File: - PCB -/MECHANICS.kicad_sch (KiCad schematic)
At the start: 4 parts, among them SW1 SW_SPDT

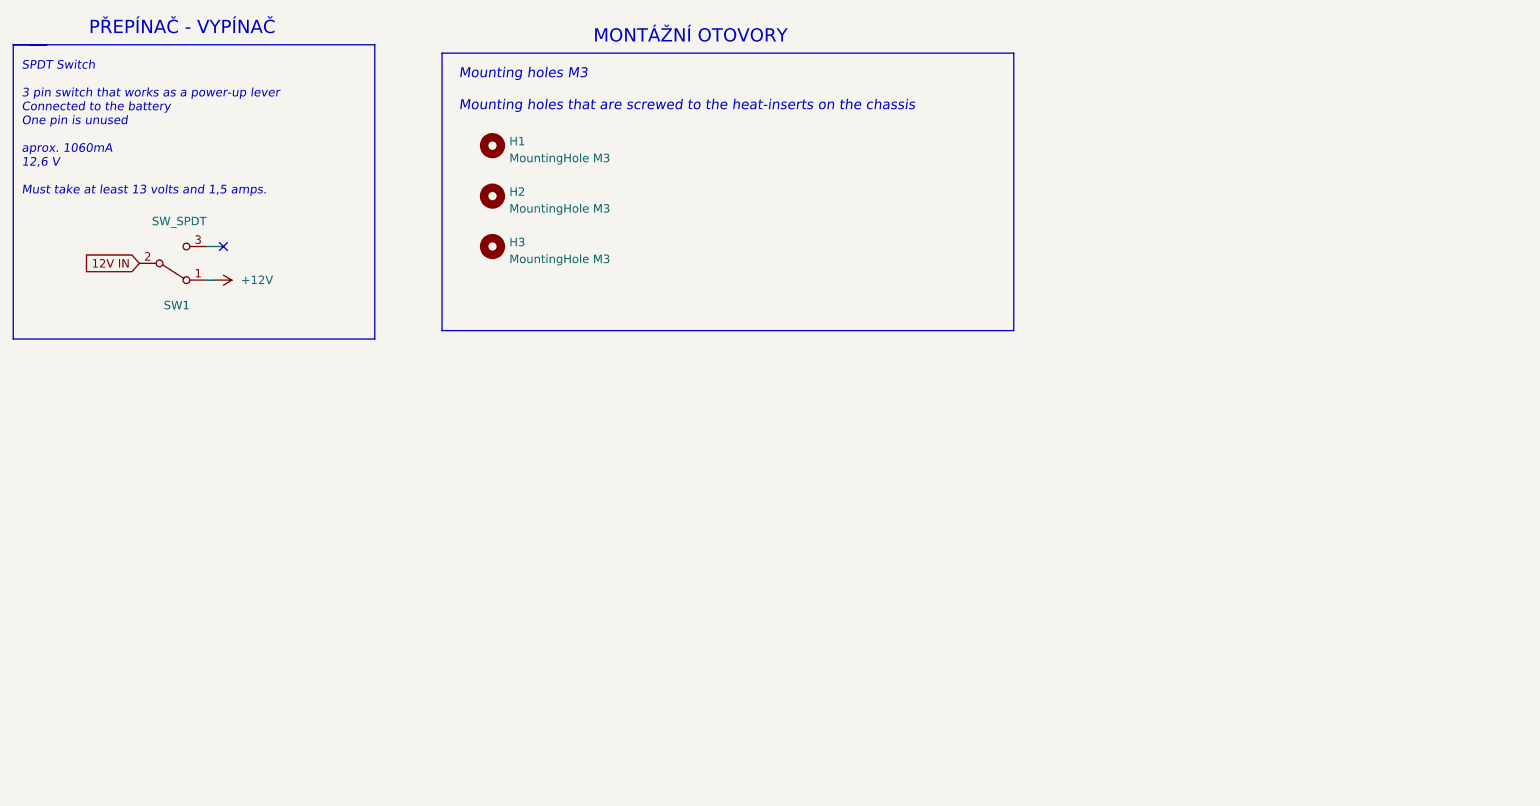
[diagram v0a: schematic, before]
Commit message: PCB - SCH UPDATE (fully labelled and described)
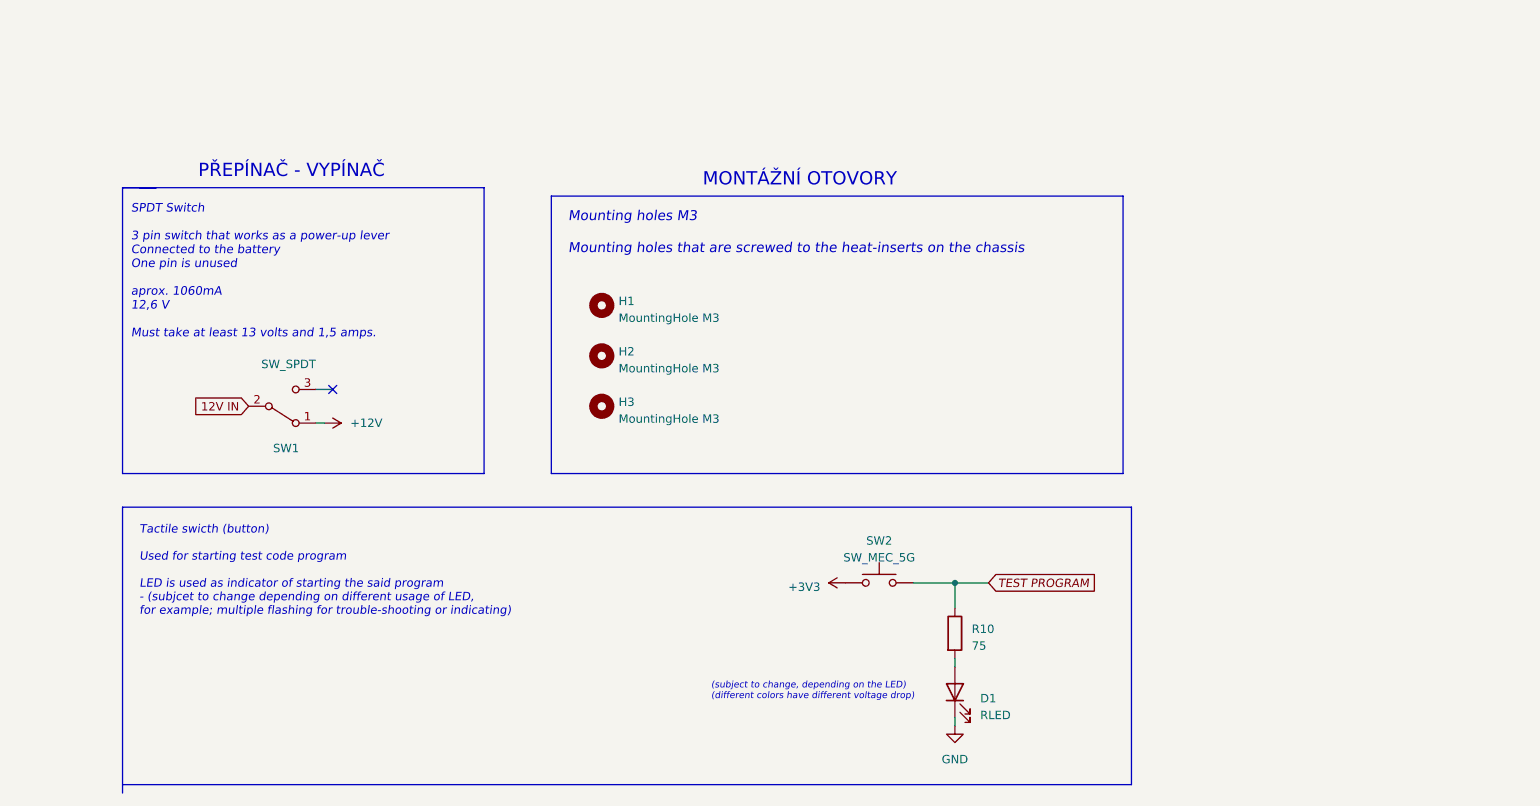
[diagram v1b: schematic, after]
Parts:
- added D1: RLED, symbol Device:LED
- added R10: 75, symbol Device:R
- added SW2: SW_MEC_5G, symbol Switch:SW_MEC_5G
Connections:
- new net: D1.2 (A), R10.2
- new net +3V3: SW2.1 (A), SW2.2 (A)
- new net GND: D1.1 (K)
- new net TEST PROGRAM: R10.1, SW2.3 (B), SW2.4 (B)
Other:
- note added: "(subject to change, depending on the LED) (different colors have different voltage drop)"
- note added: "Tactile swicth (button) Used for starting test code program LED is used as indicator of starting the said program - (subjcet to change depending on different usage of LED, for example; multiple flashing for trouble-shooting or indicating)"
- moved on the sheet: H1, H2, H3, SW1

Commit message: PCB - sch and footprint update, QRE1113 3D model.
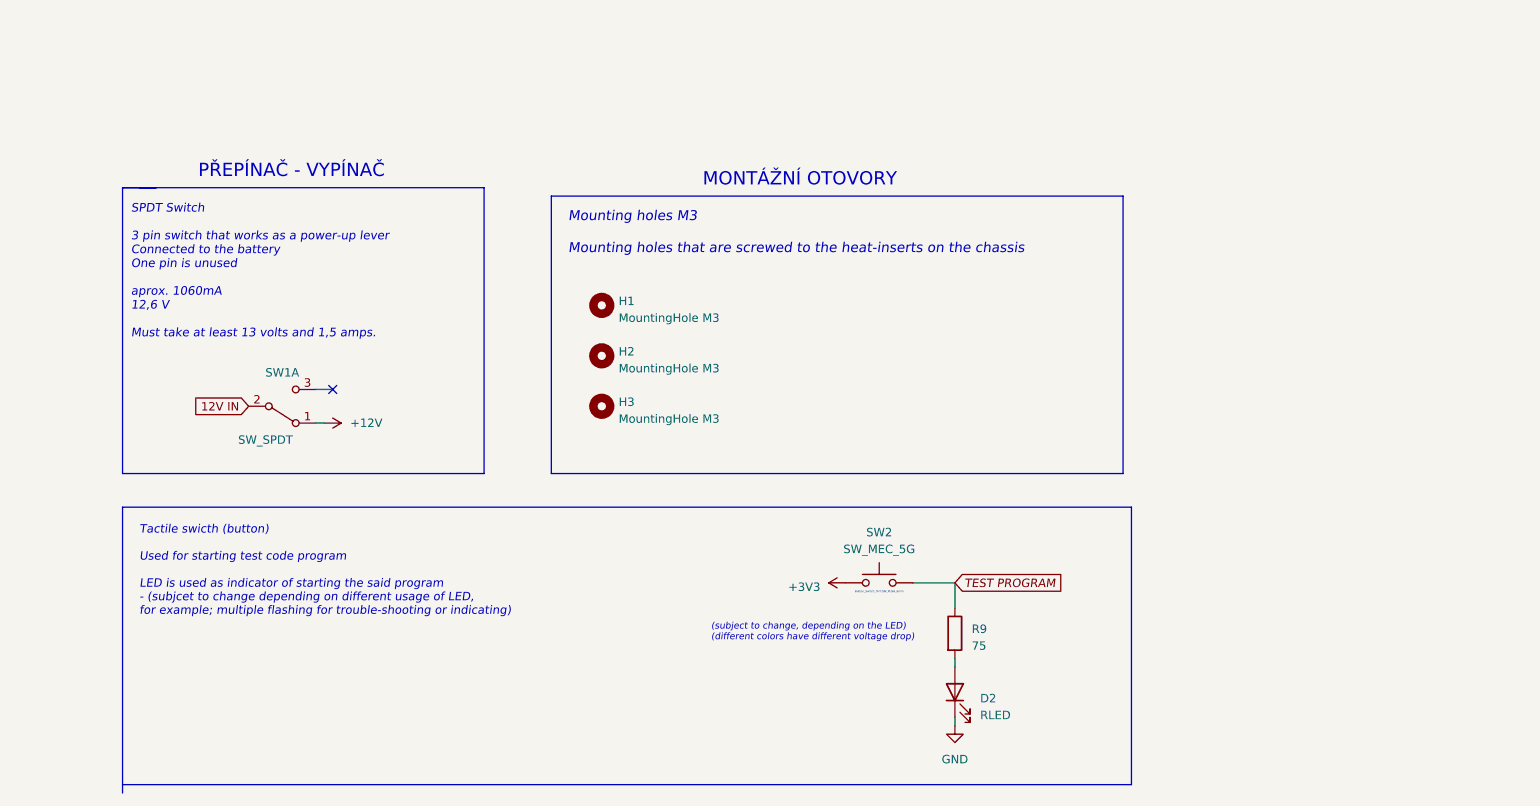
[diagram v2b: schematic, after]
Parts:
- removed SW1: SW_SPDT, SWITCH:SW_100SP1T1B4M2QE, symbol Switch:SW_SPDT
- added SW1: SW_SPDT, SWITCH SPDT:SW_100SP1T1B4M2QE, symbol Switch:SW_DPDT_x2
- D2: renamed from D1; footprint (none) -> LED_THT:LED_D5.0mm
- R9: renamed from R10; footprint (none) -> Resistor_THT:R_Axial_DIN0207_L6.3mm_D2.5mm_P10.16mm_Horizontal
- SW2: footprint (none) -> Button_Switch_THT:SW_PUSH_6mm
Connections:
- net +12V: now also SW1.1 (A)
- net 12V IN: now also SW1.2 (B)
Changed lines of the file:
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@@
 (kicad_sch (version 20230121) (generator eeschema)
   (paper "A4")
-  (junction (at 191.77 127) (diameter 0) (color 0 0 0 0)
-  )
   (no_connect (at 97.79 97.79))
   (polyline (pts (xy 66.04 115.57) (xy 218.44 115.57))
     (stroke (width 0) (type default))
   )
-  (wire (pts (xy 191.77 130.81) (xy 191.77 127))
-    (stroke (width 0) (type default))
-  )
   (wire (pts (xy 191.77 147.32) (xy 191.77 148.59))
     (stroke (width 0) (type default))
@@
     (stroke (width 0) (type default))
   )
+  (wire (pts (xy 191.77 127) (xy 191.77 130.81))
+    (stroke (width 0) (type default))
+  )
   (polyline (pts (xy 130.81 68.58) (xy 217.17 68.58))
     (stroke (width 0) (type default))
   )
   (wire (pts (xy 191.77 127) (xy 185.42 127))
-    (stroke (width 0) (type default))
-  )
-  (wire (pts (xy 196.85 127) (xy 191.77 127))
     (stroke (width 0) (type default))
   )
@@
   )
   (text "(subject to change, depending on the LED)\n(different colors have different voltage drop)"
-    (at 154.94 144.78 0)
+    (at 154.94 135.89 0)
     (effects (font (size 1 1) italic) (justify left bottom))
   )
-  (global_label "TEST PROGRAM" (shape input) (at 196.85 127 0) (fields_autoplaced)
+  (global_label "TEST PROGRAM" (shape input) (at 191.77 127 0) (fields_autoplaced)
     (effects (font (size 1.27 1.27) italic) (justify left))
-    (property "Intersheetrefs" "${INTERSHEET_REFS}" (at 213.8845 127 0)
+    (property "Intersheetrefs" "${INTERSHEET_REFS}" (at 208.8045 127 0)
       (effects (font (size 1.27 1.27)) (justify left) hide)
     )
@@
   )
   (symbol (lib_id "Switch:SW_MEC_5G") (at 180.34 127 0) (unit 1)
-    (in_bom yes) (on_board yes) (dnp no) (fields_autoplaced)
-    (property "Reference" "SW2" (at 180.34 120.65 0)
-      (effects (font (size 1.27 1.27)))
-    )
-    (property "Value" "SW_MEC_5G" (at 180.34 123.19 0)
-      (effects (font (size 1.27 1.27)))
-    )
-    (property "Footprint" "" (at 180.34 121.92 0)
-      (effects (font (size 1.27 1.27)) hide)
+    (in_bom yes) (on_board yes) (dnp no)
+    (property "Reference" "SW2" (at 180.34 119.38 0)
+      (effects (font (size 1.27 1.27)))
+    )
+    (property "Value" "SW_MEC_5G" (at 180.34 121.92 0)
+      (effects (font (size 1.27 1.27)))
+    )
+    (property "Footprint" "Button_Switch_THT:SW_PUSH_6mm" (at 180.34 128.27 0)
+      (effects (font (size 0.3 0.3)))
     )
     (property "Datasheet" "http://www.apem.com/int/index.php?controller=attachment&id_attachment=488" (at 180.34 121.92 0)
@@
   (symbol (lib_id "Device:R") (at 191.77 134.62 0) (unit 1)
     (in_bom yes) (on_board yes) (dnp no) (fields_autoplaced)
-    (property "Reference" "R10" (at 194.31 133.985 0)
+    (property "Reference" "R9" (at 194.31 133.985 0)
       (effects (font (size 1.27 1.27)) (justify left))
     )
@@
       (effects (font (size 1.27 1.27)) (justify left))
     )
-    (property "Footprint" "" (at 189.992 134.62 90)
+    (property "Footprint" "Resistor_THT:R_Axial_DIN0207_L6.3mm_D2.5mm_P10.16mm_Horizontal" (at 189.992 134.62 90)
       (effects (font (size 1.27 1.27)) hide)
     )
@@
       (project "sumec"
         (path "/fc70a1a8-ed7c-4a0f-9b1a-f23293528385/05a35bad-c108-46ad-8f95-76319a60a14f"
-          (reference "R10") (unit 1)
-        )
-      )
-    )
-  )
-  (symbol (lib_id "Switch:SW_SPDT") (at 90.17 100.33 0) (mirror x) (unit 1)
-    (in_bom yes) (on_board yes) (dnp no)
-    (property "Reference" "SW1" (at 92.71 106.68 0)
-      (effects (font (size 1.27 1.27)) (justify right))
-    )
-    (property "Value" "SW_SPDT" (at 95.25 93.98 0)
-      (effects (font (size 1.27 1.27)) (justify right))
-    )
-    (property "Footprint" "SWITCH:SW_100SP1T1B4M2QE" (at 90.17 100.33 0)
-      (effects (font (size 1.27 1.27)) hide)
-    )
-    (property "Datasheet" "~" (at 90.17 100.33 0)
-      (effects (font (size 1.27 1.27)) hide)
-    )
-    (pin "1")
-    (pin "2")
-    (pin "3")
-    (instances
-      (project "sumec"
-        (path "/fc70a1a8-ed7c-4a0f-9b1a-f23293528385"
-          (reference "SW1") (unit 1)
-        )
-        (path "/fc70a1a8-ed7c-4a0f-9b1a-f23293528385/05a35bad-c108-46ad-8f95-76319a60a14f"
-          (reference "SW1") (unit 1)
+          (reference "R9") (unit 1)
         )
       )
@@
     )
   )
+  (symbol (lib_id "Switch:SW_DPDT_x2") (at 90.17 100.33 0) (mirror x) (unit 1)
+    (in_bom yes) (on_board yes) (dnp no)
+    (property "Reference" "SW1" (at 90.17 95.25 0)
+      (effects (font (size 1.27 1.27)))
+    )
+    (property "Value" "SW_SPDT" (at 87.63 105.41 0)
+      (effects (font (size 1.27 1.27)))
+    )
+    (property "Footprint" "SWITCH SPDT:SW_100SP1T1B4M2QE" (at 90.17 100.33 0)
+      (effects (font (size 1.27 1.27)) hide)
+    )
+    (property "Datasheet" "~" (at 90.17 100.33 0)
+      (effects (font (size 1.27 1.27)) hide)
+    )
+    (pin "1")
+    (pin "2")
+    (pin "3")
+    (pin "4")
+    (pin "5")
+    (pin "6")
+    (instances
+      (project "sumec"
+        (path "/fc70a1a8-ed7c-4a0f-9b1a-f23293528385/05a35bad-c108-46ad-8f95-76319a60a14f"
+          (reference "SW1") (unit 1)
+        )
+      )
+    )
+  )
   (symbol (lib_id "Device:LED") (at 191.77 143.51 90) (unit 1)
     (in_bom yes) (on_board yes) (dnp no) (fields_autoplaced)
-    (property "Reference" "D1" (at 195.58 144.4625 90)
+    (property "Reference" "D2" (at 195.58 144.4625 90)
       (effects (font (size 1.27 1.27)) (justify right))
     )
@@
       (effects (font (size 1.27 1.27)) (justify right))
     )
-    (property "Footprint" "" (at 191.77 143.51 0)
+    (property "Footprint" "LED_THT:LED_D5.0mm" (at 191.77 143.51 0)
       (effects (font (size 1.27 1.27)) hide)
     )
@@
       (project "sumec"
         (path "/fc70a1a8-ed7c-4a0f-9b1a-f23293528385/05a35bad-c108-46ad-8f95-76319a60a14f"
-          (reference "D1") (unit 1)
-        )
-      )
+          (reference "D2") (unit 1)
+        )
+      )

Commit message: PCB - board update + footprint/3d models export
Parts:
- removed SW2: SW_MEC_5G, Button_Switch_THT:SW_PUSH_6mm, symbol Switch:SW_MEC_5G
- added SW3: SW_Push, Button_Switch_THT:SW_PUSH_6mm, symbol Switch:SW_Push
- SW1: footprint SWITCH SPDT:SW_100SP1T1B4M2QE -> Connector_JST:JST_EH_B3B-EH-A_1x03_P2.50mm_Vertical
- renumbered D2 to D1, H2 to H?, H3 to H?, H1 to H?, R9 to R1
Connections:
- net +3V3: now also SW3.1
- net TEST PROGRAM: now also SW3.2

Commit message: Board update
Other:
- note added: "^ (subject to change, depending on the LED) (different colors have different voltage drop)"
- note removed: "(subject to change, depending on the LED) (different colors have different voltage drop)"
- moved on the sheet: D1, R1, SW3
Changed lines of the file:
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@@
 (kicad_sch (version 20230121) (generator eeschema)
   (paper "A4")
+  (junction (at 173.99 139.7) (diameter 0) (color 0 0 0 0)
+  )
   (no_connect (at 97.79 97.79))
   (polyline (pts (xy 66.04 115.57) (xy 218.44 115.57))
     (stroke (width 0) (type default))
   )
-  (wire (pts (xy 191.77 147.32) (xy 191.77 148.59))
+  (wire (pts (xy 193.04 139.7) (xy 194.31 139.7))
     (stroke (width 0) (type default))
   )
@@
     (stroke (width 0) (type default))
   )
-  (wire (pts (xy 191.77 139.7) (xy 191.77 138.43))
-    (stroke (width 0) (type default))
-  )
-  (wire (pts (xy 191.77 127) (xy 191.77 130.81))
+  (wire (pts (xy 185.42 139.7) (xy 184.15 139.7))
     (stroke (width 0) (type default))
   )
@@
     (stroke (width 0) (type default))
   )
-  (wire (pts (xy 173.99 127) (xy 175.26 127))
+  (wire (pts (xy 161.29 139.7) (xy 162.56 139.7))
     (stroke (width 0) (type default))
   )
@@
     (stroke (width 0) (type default))
   )
-  (wire (pts (xy 191.77 127) (xy 185.42 127))
+  (wire (pts (xy 173.99 139.7) (xy 176.53 139.7))
+    (stroke (width 0) (type default))
+  )
+  (wire (pts (xy 172.72 139.7) (xy 173.99 139.7))
+    (stroke (width 0) (type default))
+  )
+  (wire (pts (xy 173.99 135.89) (xy 173.99 139.7))
     (stroke (width 0) (type default))
   )
@@
     (effects (font (size 1.27 1.27) italic) (justify left bottom))
   )
-  (text "(subject to change, depending on the LED)\n(different colors have different voltage drop)"
-    (at 154.94 135.89 0)
+  (text "                 ^\n(subject to change, depending on the LED)\n(different colors have different voltage drop)"
+    (at 167.64 146.05 0)
     (effects (font (size 1 1) italic) (justify left bottom))
   )
-  (global_label "TEST PROGRAM" (shape input) (at 191.77 127 0) (fields_autoplaced)
+  (global_label "TEST PROGRAM" (shape input) (at 173.99 135.89 90) (fields_autoplaced)
     (effects (font (size 1.27 1.27) italic) (justify left))
-    (property "Intersheetrefs" "${INTERSHEET_REFS}" (at 208.8045 127 0)
+    (property "Intersheetrefs" "${INTERSHEET_REFS}" (at 173.99 118.8555 90)
       (effects (font (size 1.27 1.27)) (justify left) hide)
     )
@@
     )
   )
-  (symbol (lib_id "power:GND") (at 191.77 148.59 0) (unit 1)
-    (in_bom yes) (on_board yes) (dnp no) (fields_autoplaced)
-    (property "Reference" "#PWR03" (at 191.77 154.94 0)
-      (effects (font (size 1.27 1.27)) hide)
-    )
-    (property "Value" "GND" (at 191.77 153.67 0)
-      (effects (font (size 1.27 1.27)))
-    )
-    (property "Footprint" "" (at 191.77 148.59 0)
-      (effects (font (size 1.27 1.27)) hide)
-    )
-    (property "Datasheet" "" (at 191.77 148.59 0)
+  (symbol (lib_id "power:GND") (at 194.31 139.7 90) (unit 1)
+    (in_bom yes) (on_board yes) (dnp no) (fields_autoplaced)
+    (property "Reference" "#PWR03" (at 200.66 139.7 0)
+      (effects (font (size 1.27 1.27)) hide)
+    )
+    (property "Value" "GND" (at 199.39 139.7 0)
+      (effects (font (size 1.27 1.27)))
+    )
+    (property "Footprint" "" (at 194.31 139.7 0)
+      (effects (font (size 1.27 1.27)) hide)
+    )
+    (property "Datasheet" "" (at 194.31 139.7 0)
       (effects (font (size 1.27 1.27)) hide)
     )
@@
     )
   )
-  (symbol (lib_id "Switch:SW_Push") (at 180.34 127 0) (unit 1)
-    (in_bom yes) (on_board yes) (dnp no) (fields_autoplaced)
-    (property "Reference" "SW3" (at 180.34 120.65 0)
-      (effects (font (size 1.27 1.27)))
-    )
-    (property "Value" "SW_Push" (at 180.34 123.19 0)
-      (effects (font (size 1.27 1.27)))
-    )
-    (property "Footprint" "Button_Switch_THT:SW_PUSH_6mm" (at 180.34 121.92 0)
-      (effects (font (size 1.27 1.27)) hide)
-    )
-    (property "Datasheet" "~" (at 180.34 121.92 0)
+  (symbol (lib_id "Switch:SW_Push") (at 167.64 139.7 0) (unit 1)
+    (in_bom yes) (on_board yes) (dnp no) (fields_autoplaced)
+    (property "Reference" "SW3" (at 167.64 133.35 0)
+      (effects (font (size 1.27 1.27)))
+    )
+    (property "Value" "SW_Push" (at 167.64 135.89 0)
+      (effects (font (size 1.27 1.27)))
+    )
+    (property "Footprint" "Button_Switch_THT:SW_PUSH_6mm" (at 167.64 134.62 0)
+      (effects (font (size 1.27 1.27)) hide)
+    )
+    (property "Datasheet" "~" (at 167.64 134.62 0)
       (effects (font (size 1.27 1.27)) hide)
     )
@@
     )
   )
-  (symbol (lib_id "power:+3V3") (at 173.99 127 90) (unit 1)
-    (in_bom yes) (on_board yes) (dnp no) (fields_autoplaced)
-    (property "Reference" "#PWR02" (at 177.8 127 0)
-      (effects (font (size 1.27 1.27)) hide)
-    )
-    (property "Value" "+3V3" (at 170.18 127.635 90)
-      (effects (font (size 1.27 1.27)) (justify left))
-    )
-    (property "Footprint" "" (at 173.99 127 0)
-      (effects (font (size 1.27 1.27)) hide)
-    )
-    (property "Datasheet" "" (at 173.99 127 0)
+  (symbol (lib_id "power:+3V3") (at 161.29 139.7 90) (unit 1)
+    (in_bom yes) (on_board yes) (dnp no) (fields_autoplaced)
+    (property "Reference" "#PWR02" (at 165.1 139.7 0)
+      (effects (font (size 1.27 1.27)) hide)
+    )
+    (property "Value" "+3V3" (at 157.48 140.335 90)
+      (effects (font (size 1.27 1.27)) (justify left))
+    )
+    (property "Footprint" "" (at 161.29 139.7 0)
+      (effects (font (size 1.27 1.27)) hide)
+    )
+    (property "Datasheet" "" (at 161.29 139.7 0)
       (effects (font (size 1.27 1.27)) hide)
     )
@@
     )
   )
-  (symbol (lib_id "Device:R") (at 191.77 134.62 0) (unit 1)
-    (in_bom yes) (on_board yes) (dnp no) (fields_autoplaced)
-    (property "Reference" "R1" (at 194.31 133.985 0)
-      (effects (font (size 1.27 1.27)) (justify left))
-    )
-    (property "Value" "75 " (at 194.31 136.525 0)
-      (effects (font (size 1.27 1.27)) (justify left))
-    )
-    (property "Footprint" "Resistor_THT:R_Axial_DIN0207_L6.3mm_D2.5mm_P10.16mm_Horizontal" (at 189.992 134.62 90)
-      (effects (font (size 1.27 1.27)) hide)
-    )
-    (property "Datasheet" "~" (at 191.77 134.62 0)
+  (symbol (lib_id "Device:R") (at 180.34 139.7 90) (unit 1)
+    (in_bom yes) (on_board yes) (dnp no) (fields_autoplaced)
+    (property "Reference" "R1" (at 179.705 137.16 0)
+      (effects (font (size 1.27 1.27)) (justify left))
+    )
+    (property "Value" "75 " (at 182.245 137.16 0)
+      (effects (font (size 1.27 1.27)) (justify left))
+    )
+    (property "Footprint" "Resistor_THT:R_Axial_DIN0207_L6.3mm_D2.5mm_P10.16mm_Horizontal" (at 180.34 141.478 90)
+      (effects (font (size 1.27 1.27)) hide)
+    )
+    (property "Datasheet" "~" (at 180.34 139.7 0)
       (effects (font (size 1.27 1.27)) hide)
     )
@@
     )
   )
-  (symbol (lib_id "Device:LED") (at 191.77 143.51 90) (unit 1)
-    (in_bom yes) (on_board yes) (dnp no) (fields_autoplaced)
-    (property "Reference" "D1" (at 195.58 144.4625 90)
+  (symbol (lib_id "Device:LED") (at 189.23 139.7 180) (unit 1)
+    (in_bom yes) (on_board yes) (dnp no) (fields_autoplaced)
+    (property "Reference" "D1" (at 190.1825 135.89 90)
       (effects (font (size 1.27 1.27)) (justify right))
     )
-    (property "Value" "RLED" (at 195.58 147.0025 90)
+    (property "Value" "RLED" (at 192.7225 135.89 90)
       (effects (font (size 1.27 1.27)) (justify right))
     )
-    (property "Footprint" "LED_THT:LED_D5.0mm" (at 191.77 143.51 0)
-      (effects (font (size 1.27 1.27)) hide)
-    )
-    (property "Datasheet" "~" (at 191.77 143.51 0)
-      (effects (font (size 1.27 1.27)) hide)
-    )
+    (property "Footprint" "LED_THT:LED_D5.0mm" (at 189.23 139.7 0)
+      (effects (font (size 1.27 1.27)) hide)
+    )
+    (property "Datasheet" "~" (at 189.23 139.7 0)
+      (effects (font (size 1.27 1.27)) hide)
+    )
